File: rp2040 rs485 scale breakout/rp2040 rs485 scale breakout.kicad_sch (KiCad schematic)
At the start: 59 parts, among them J1 main i2c, J10 i2c 3, J11 i2c 4, J12 i2c 2, J13 i2c 0, J14 i2c 1, J2 ESDU5V0H4, J3 rs485, J4 Conn_01x01, J5 i2c pullups, J6 qwiic from pro micro, J7 i2c 5, J8 i2c 6, J9 i2c 7, U1 MAX487E, U2 ProMicro_2040, U3 PCA9548ADW

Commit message: motor driver and scale pcb gerbers
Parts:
- added C24, C25: 10uF, Capacitor_SMD:C_1206_3216Metric, symbol Device:C
- added D1: 24v, LED_SMD:LED_0603_1608Metric, symbol Device:LED
- added D2: 5v, LED_SMD:LED_0603_1608Metric, symbol Device:LED
- added D3: 3.3v, LED_SMD:LED_0603_1608Metric, symbol Device:LED
- added J23: power in, TerminalBlock_Phoenix:TerminalBlock_Phoenix_MKDS-1,5-2_1x02_P5.00mm_Horizontal, symbol Connector_Generic:Conn_01x02
- added R41, R42, R43: 2.2K, Resistor_SMD:R_0603_1608Metric, symbol Device:R
- added U6: mp1584 dcdc, Evan's misc parts:MP1584_buck_module, symbol Connector_Generic:Conn_01x04
- added U7: LD1117S33, Package_TO_SOT_SMD:SOT-223-3_TabPin2, symbol Regulator_Linear:LD1117S33TR_SOT223
- U3: footprint Evan's misc parts:SOIC127P1030X265-24N -> Package_SO:TSSOP-24_4.4x7.8mm_P0.65mm
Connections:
- net +3V3: now also C25.1, R43.1, U7.2 (VO)
- net GND: now also C24.2, C25.2, D1.1 (K), D2.1 (K), D3.1 (K), J23.1 (Pin_1), U6.2 (Pin_2), U6.3 (Pin_3), U7.1 (GND)
- new net: D1.2 (A), R41.2
- new net: D2.2 (A), R42.2
- new net: D3.2 (A), R43.2
- new net +24V: J23.2 (Pin_2), R41.1, U6.1 (Pin_1)
- new net +5V: C24.1, R42.1, U6.4 (Pin_4), U7.3 (VI)
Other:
- note added: "in +"
- note added: "in -"
- note added: "out +"
- note added: "out -"
- moved on the sheet: J1, U2

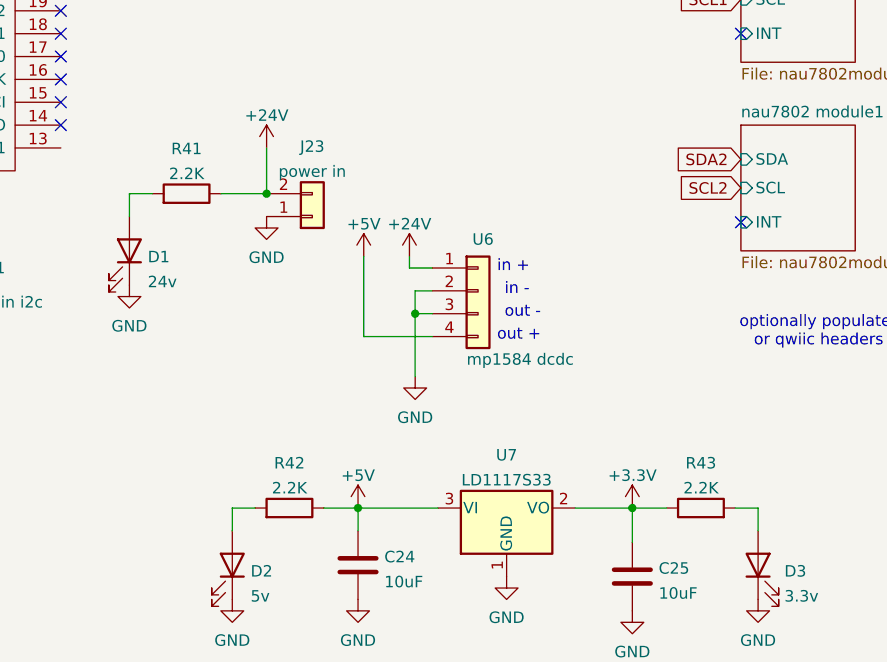
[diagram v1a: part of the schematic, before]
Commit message: created scart TV breakout, revised motor controller and scale board for manufacturing
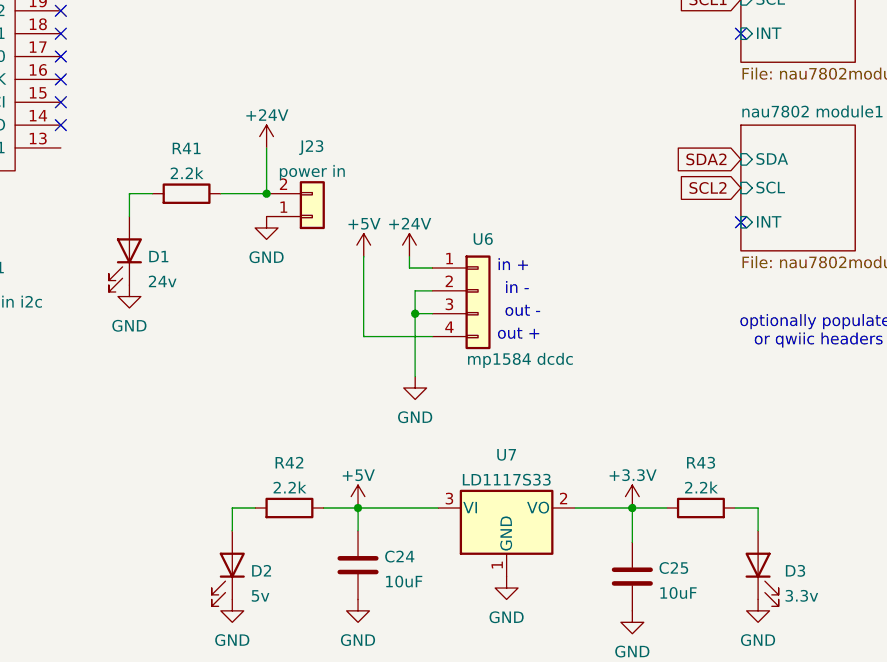
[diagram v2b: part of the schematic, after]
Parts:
- R41, R42, R43: value 2.2K -> 2.2k
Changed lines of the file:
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@@
     (in_bom yes) (on_board yes) (fields_autoplaced)
     (property "Reference" "R41" (id 0) (at 85.725 132.1775 90))
-    (property "Value" "2.2K" (id 1) (at 85.725 134.9526 90))
+    (property "Value" "2.2k" (id 1) (at 85.725 134.9526 90))
     (property "Footprint" "Resistor_SMD:R_0603_1608Metric" (id 2) (at 85.725 138.938 90)
       (effects (font (size 1.27 1.27)) hide)
@@
     (in_bom yes) (on_board yes) (fields_autoplaced)
     (property "Reference" "R43" (id 0) (at 142.875 167.1025 90))
-    (property "Value" "2.2K" (id 1) (at 142.875 169.8776 90))
+    (property "Value" "2.2k" (id 1) (at 142.875 169.8776 90))
     (property "Footprint" "Resistor_SMD:R_0603_1608Metric" (id 2) (at 142.875 173.863 90)
       (effects (font (size 1.27 1.27)) hide)
@@
     (in_bom yes) (on_board yes) (fields_autoplaced)
     (property "Reference" "R42" (id 0) (at 97.155 167.1025 90))
-    (property "Value" "2.2K" (id 1) (at 97.155 169.8776 90))
+    (property "Value" "2.2k" (id 1) (at 97.155 169.8776 90))
     (property "Footprint" "Resistor_SMD:R_0603_1608Metric" (id 2) (at 97.155 173.863 90)
       (effects (font (size 1.27 1.27)) hide)
@@
     )
     (path "/996e9b76-83f8-44ca-8664-6b933f11f1d6"
-      (reference "R41") (unit 1) (value "2.2K") (footprint "Resistor_SMD:R_0603_1608Metric")
+      (reference "R41") (unit 1) (value "2.2k") (footprint "Resistor_SMD:R_0603_1608Metric")
     )
     (path "/d0e725ea-0733-4bc0-a1e1-81b399c8aa63"
-      (reference "R42") (unit 1) (value "2.2K") (footprint "Resistor_SMD:R_0603_1608Metric")
+      (reference "R42") (unit 1) (value "2.2k") (footprint "Resistor_SMD:R_0603_1608Metric")
     )
     (path "/bb94ae00-688a-4310-a322-04330d8ac135"
-      (reference "R43") (unit 1) (value "2.2K") (footprint "Resistor_SMD:R_0603_1608Metric")
+      (reference "R43") (unit 1) (value "2.2k") (footprint "Resistor_SMD:R_0603_1608Metric")
     )
     (path "/6ed7094b-12de-4d09-93e1-25c1d8fc4744"

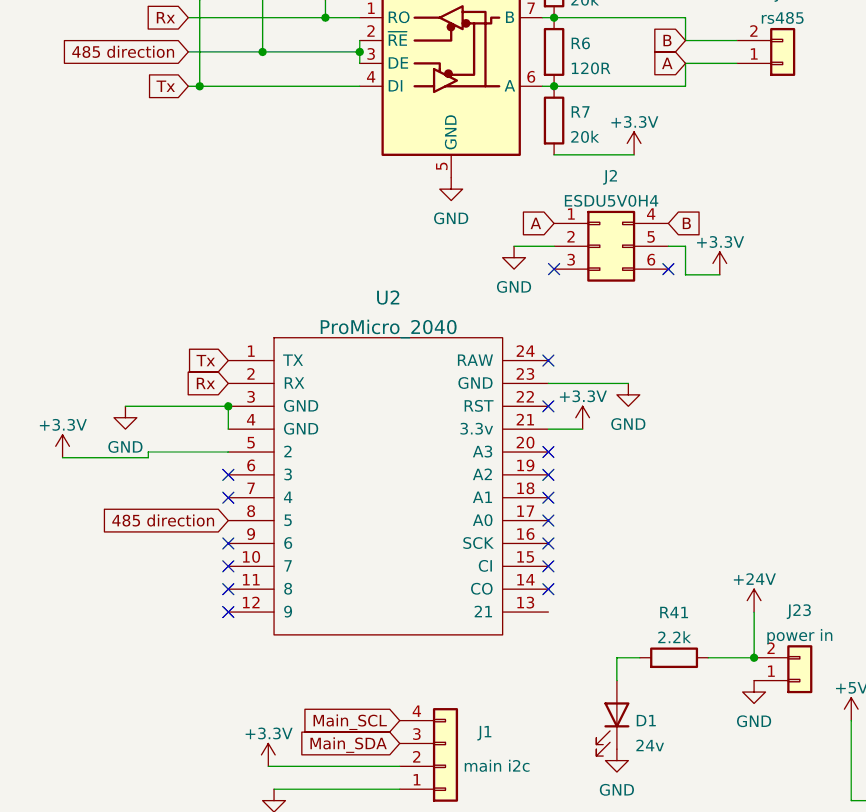
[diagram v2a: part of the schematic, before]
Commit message: tweaked buck converter hole sizes and silk
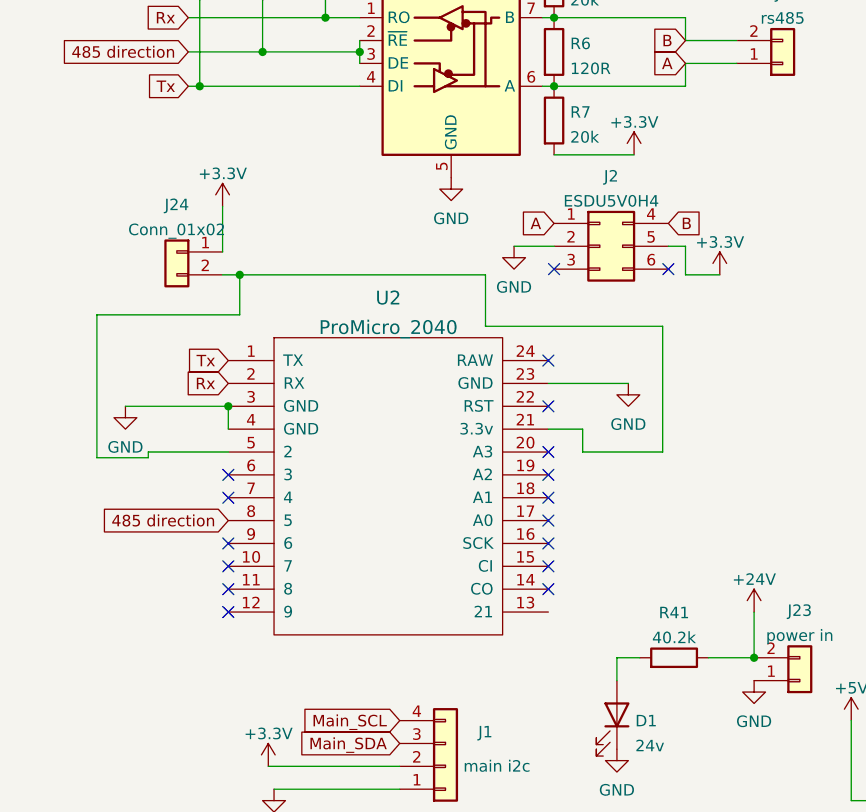
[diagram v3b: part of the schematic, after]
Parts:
- added J24: Conn_01x02, Connector_PinHeader_2.54mm:PinHeader_2x01_P2.54mm_Vertical, symbol Connector_Generic:Conn_01x02
- R41: value 2.2k -> 40.2k
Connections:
- net +3V3: now also J24.1 (Pin_1); no longer U2.21 (3.3v), U2.5 (2)
- new net: J24.2 (Pin_2), U2.21 (3.3v), U2.5 (2)
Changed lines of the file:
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@@
   (junction (at 72.39 20.32) (diameter 0) (color 0 0 0 0)
   )
+  (junction (at 37.465 94.615) (diameter 0) (color 0 0 0 0)
+  )
   (junction (at 249.555 30.48) (diameter 0) (color 0 0 0 0)
   )
@@
     (stroke (width 0) (type default) (color 0 0 0 0))
   )
+  (wire (pts (xy 84.455 114.3) (xy 75.565 114.3))
+    (stroke (width 0) (type default) (color 0 0 0 0))
+  )
   (wire (pts (xy 45.72 29.21) (xy 54.61 29.21))
     (stroke (width 0) (type default) (color 0 0 0 0))
@@
     (stroke (width 0) (type default) (color 0 0 0 0))
   )
+  (wire (pts (xy 35.56 94.615) (xy 37.465 94.615))
+    (stroke (width 0) (type default) (color 0 0 0 0))
+  )
   (wire (pts (xy 72.39 20.32) (xy 64.77 20.32))
     (stroke (width 0) (type default) (color 0 0 0 0))
@@
     (stroke (width 0) (type default) (color 0 0 0 0))
   )
+  (wire (pts (xy 154.305 20.32) (xy 154.305 34.29))
+    (stroke (width 0) (type default) (color 0 0 0 0))
+  )
   (wire (pts (xy 31.75 69.85) (xy 40.005 69.85))
     (stroke (width 0) (type default) (color 0 0 0 0))
@@
     (stroke (width 0) (type default) (color 0 0 0 0))
   )
+  (wire (pts (xy 75.565 114.3) (xy 75.565 111.76))
+    (stroke (width 0) (type default) (color 0 0 0 0))
+  )
   (wire (pts (xy 247.65 106.68) (xy 247.65 107.95))
     (stroke (width 0) (type default) (color 0 0 0 0))
@@
     (stroke (width 0) (type default) (color 0 0 0 0))
   )
+  (wire (pts (xy 37.465 94.615) (xy 64.77 94.615))
+    (stroke (width 0) (type default) (color 0 0 0 0))
+  )
   (wire (pts (xy 118.745 24.13) (xy 118.745 20.32))
     (stroke (width 0) (type default) (color 0 0 0 0))
@@
     (stroke (width 0) (type default) (color 0 0 0 0))
   )
+  (wire (pts (xy 84.455 100.33) (xy 84.455 114.3))
+    (stroke (width 0) (type default) (color 0 0 0 0))
+  )
   (wire (pts (xy 33.02 64.135) (xy 33.02 73.66))
     (stroke (width 0) (type default) (color 0 0 0 0))
@@
     (stroke (width 0) (type default) (color 0 0 0 0))
   )
-  (wire (pts (xy 27.305 114.935) (xy 17.78 114.935))
+  (wire (pts (xy 27.305 114.935) (xy 21.59 114.935))
     (stroke (width 0) (type default) (color 0 0 0 0))
   )
@@
     (stroke (width 0) (type default) (color 0 0 0 0))
   )
+  (wire (pts (xy 64.77 94.615) (xy 64.77 100.33))
+    (stroke (width 0) (type default) (color 0 0 0 0))
+  )
   (wire (pts (xy 179.07 41.91) (xy 193.04 41.91))
     (stroke (width 0) (type default) (color 0 0 0 0))
@@
     (stroke (width 0) (type default) (color 0 0 0 0))
   )
+  (wire (pts (xy 64.77 100.33) (xy 84.455 100.33))
+    (stroke (width 0) (type default) (color 0 0 0 0))
+  )
   (wire (pts (xy 172.085 29.845) (xy 172.085 20.32))
     (stroke (width 0) (type default) (color 0 0 0 0))
@@
     (stroke (width 0) (type default) (color 0 0 0 0))
   )
-  (wire (pts (xy 154.305 20.32) (xy 154.305 34.29))
-    (stroke (width 0) (type default) (color 0 0 0 0))
-  )
   (wire (pts (xy 245.11 110.49) (xy 255.27 110.49))
     (stroke (width 0) (type default) (color 0 0 0 0))
@@
     (stroke (width 0) (type default) (color 0 0 0 0))
   )
+  (wire (pts (xy 21.59 99.06) (xy 37.465 99.06))
+    (stroke (width 0) (type default) (color 0 0 0 0))
+  )
   (wire (pts (xy 149.225 174.625) (xy 149.225 172.085))
     (stroke (width 0) (type default) (color 0 0 0 0))
@@
     (stroke (width 0) (type default) (color 0 0 0 0))
   )
+  (wire (pts (xy 37.465 99.06) (xy 37.465 94.615))
+    (stroke (width 0) (type default) (color 0 0 0 0))
+  )
   (wire (pts (xy 206.375 67.31) (xy 206.375 71.12))
     (stroke (width 0) (type default) (color 0 0 0 0))
   )
+  (wire (pts (xy 21.59 114.935) (xy 21.59 99.06))
+    (stroke (width 0) (type default) (color 0 0 0 0))
+  )
   (wire (pts (xy 248.92 78.74) (xy 248.92 80.01))
     (stroke (width 0) (type default) (color 0 0 0 0))
@@
     (stroke (width 0) (type default) (color 0 0 0 0))
   )
+  (wire (pts (xy 35.56 86.995) (xy 35.56 92.075))
+    (stroke (width 0) (type default) (color 0 0 0 0))
+  )
   (wire (pts (xy 31.75 73.66) (xy 33.02 73.66))
     (stroke (width 0) (type default) (color 0 0 0 0))
@@
     (pin "2")
   )
-  (symbol (lib_id "power:+3.3V") (at 75.565 111.76 0) (unit 1)
-    (in_bom yes) (on_board yes) (fields_autoplaced)
-    (property "Reference" "#PWR014" (id 0) (at 75.565 115.57 0)
-      (effects (font (size 1.27 1.27)) hide)
-    )
-    (property "Value" "+3.3V" (id 1) (at 75.565 108.1555 0))
-    (property "Footprint" "" (id 2) (at 75.565 111.76 0)
-      (effects (font (size 1.27 1.27)) hide)
-    )
-    (property "Datasheet" "" (id 3) (at 75.565 111.76 0)
-      (effects (font (size 1.27 1.27)) hide)
-    )
-    (pin "1")
-  )
   (symbol (lib_id "power:+3.3V") (at 253.365 46.355 0) (unit 1)
     (in_bom yes) (on_board yes) (fields_autoplaced)
@@
     (pin "1")
   )
+  (symbol (lib_id "power:+3.3V") (at 35.56 86.995 0) (unit 1)
+    (in_bom yes) (on_board yes) (fields_autoplaced)
+    (property "Reference" "#PWR0101" (id 0) (at 35.56 90.805 0)
+      (effects (font (size 1.27 1.27)) hide)
+    )
+    (property "Value" "+3.3V" (id 1) (at 35.56 83.3905 0))
+    (property "Footprint" "" (id 2) (at 35.56 86.995 0)
+      (effects (font (size 1.27 1.27)) hide)
+    )
+    (property "Datasheet" "" (id 3) (at 35.56 86.995 0)
+      (effects (font (size 1.27 1.27)) hide)
+    )
+    (pin "1")
+  )
   (symbol (lib_id "Device:LED") (at 90.805 178.435 270) (mirror x) (unit 1)
     (in_bom yes) (on_board yes) (fields_autoplaced)
@@
     (in_bom yes) (on_board yes) (fields_autoplaced)
     (property "Reference" "R41" (id 0) (at 85.725 132.1775 90))
-    (property "Value" "2.2k" (id 1) (at 85.725 134.9526 90))
+    (property "Value" "40.2k" (id 1) (at 85.725 134.9526 90))
     (property "Footprint" "Resistor_SMD:R_0603_1608Metric" (id 2) (at 85.725 138.938 90)
       (effects (font (size 1.27 1.27)) hide)
@@
     (pin "2")
   )
+  (symbol (lib_id "Connector_Generic:Conn_01x02") (at 30.48 92.075 0) (mirror y) (unit 1)
+    (in_bom yes) (on_board yes) (fields_autoplaced)
+    (property "Reference" "J24" (id 0) (at 30.48 86.8385 0))
+    (property "Value" "Conn_01x02" (id 1) (at 30.48 89.6136 0))
+    (property "Footprint" "Connector_PinHeader_2.54mm:PinHeader_2x01_P2.54mm_Vertical" (id 2) (at 30.48 92.075 0)
+      (effects (font (size 1.27 1.27)) hide)
+    )
+    (property "Datasheet" "~" (id 3) (at 30.48 92.075 0)
+      (effects (font (size 1.27 1.27)) hide)
+    )
+    (pin "1")
+    (pin "2")
+  )
   (symbol (lib_id "Device:R") (at 72.39 77.47 0) (unit 1)
     (in_bom yes) (on_board yes) (fields_autoplaced)
@@
     (pin "2")
   )
-  (symbol (lib_id "power:+3.3V") (at 17.78 114.935 0) (unit 1)
-    (in_bom yes) (on_board yes) (fields_autoplaced)
-    (property "Reference" "#PWR0101" (id 0) (at 17.78 118.745 0)
-      (effects (font (size 1.27 1.27)) hide)
-    )
-    (property "Value" "+3.3V" (id 1) (at 17.78 111.3305 0))
-    (property "Footprint" "" (id 2) (at 17.78 114.935 0)
-      (effects (font (size 1.27 1.27)) hide)
-    )
-    (property "Datasheet" "" (id 3) (at 17.78 114.935 0)
-      (effects (font (size 1.27 1.27)) hide)
-    )
-    (pin "1")
-  )
   (symbol (lib_id "Device:R") (at 247.65 102.87 0) (unit 1)
     (in_bom yes) (on_board yes) (fields_autoplaced)
@@
       (reference "#PWR013") (unit 1) (value "+3.3V") (footprint "")
     )
-    (path "/4fa3a388-fdb3-43d6-a918-2f34caeb1131"
-      (reference "#PWR014") (unit 1) (value "+3.3V") (footprint "")
-    )
     (path "/093449f1-5c05-47f1-8efc-85179d5593cd"
       (reference "#PWR015") (unit 1) (value "GND") (footprint "")
@@
       (reference "#PWR092") (unit 1) (value "GND") (footprint "")
     )
-    (path "/e91a23c0-b3ea-47ba-b6f4-1dd0380fabe4"
+    (path "/551b88fb-7fed-4287-98ee-bbec7ae40bb2"
       (reference "#PWR0101") (unit 1) (value "+3.3V") (footprint "")
     )
@@
       (reference "J23") (unit 1) (value "power in") (footprint "TerminalBlock_Phoenix:TerminalBlock_Phoenix_MKDS-1,5-2_1x02_P5.00mm_Horizontal")
     )
+    (path "/b68372c0-f5c3-48de-972a-c29b85bdeb68"
+      (reference "J24") (unit 1) (value "Conn_01x02") (footprint "Connector_PinHeader_2.54mm:PinHeader_2x01_P2.54mm_Vertical")
+    )
     (path "/aee10841-61a6-4ee8-9326-c45dc47c5251"
       (reference "JP1") (unit 1) (value "Jumper_2_Open") (footprint "Jumper:SolderJumper-2_P1.3mm_Open_RoundedPad1.0x1.5mm")
@@
     )
     (path "/996e9b76-83f8-44ca-8664-6b933f11f1d6"
-      (reference "R41") (unit 1) (value "2.2k") (footprint "Resistor_SMD:R_0603_1608Metric")
+      (reference "R41") (unit 1) (value "40.2k") (footprint "Resistor_SMD:R_0603_1608Metric")
     )
     (path "/d0e725ea-0733-4bc0-a1e1-81b399c8aa63"
